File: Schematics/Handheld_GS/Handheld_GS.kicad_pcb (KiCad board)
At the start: 2 copper layers, 141.6 x 70 mm, 152 parts, among them IC1 P3T1755DPZ, J1 MB_A, J2 MB_B, J4 1S Li-Ion Cell, J5 Speaker, J6 MB_A, J7 1S Li-Ion Cell, J9 DB_B, Q1 AO3401A, Q2 MMBT3904, Q3 MMBT3904, Q4 AO3400A, Q5 AO3400A, Q6 AO3401A, Q7 AO3401A, SW1 SW_ENTER, SW2 SW_BACK, SW3 SW_DOWN, SW4 SW_UP, SW5 SW_ESP_BOOT_MODE, SW6 SW_ESP_RESET, SW7 PWR, U1 CP2102N-Axx-xQFN28, U10 TPB4056B2X-ES1R, U11 AMS1117-3.3, U12 NAU7802SGI, U2 ESP32-S3-WROOM-1, U3 RFM95W-915S2, U4 TPS63001DRCR, U5 LM66100DCKR, U6 LM66100DCKR, U7 MAX98357AETE_T, U8 TPS63001DRCR, U9 AMS1117-3.3

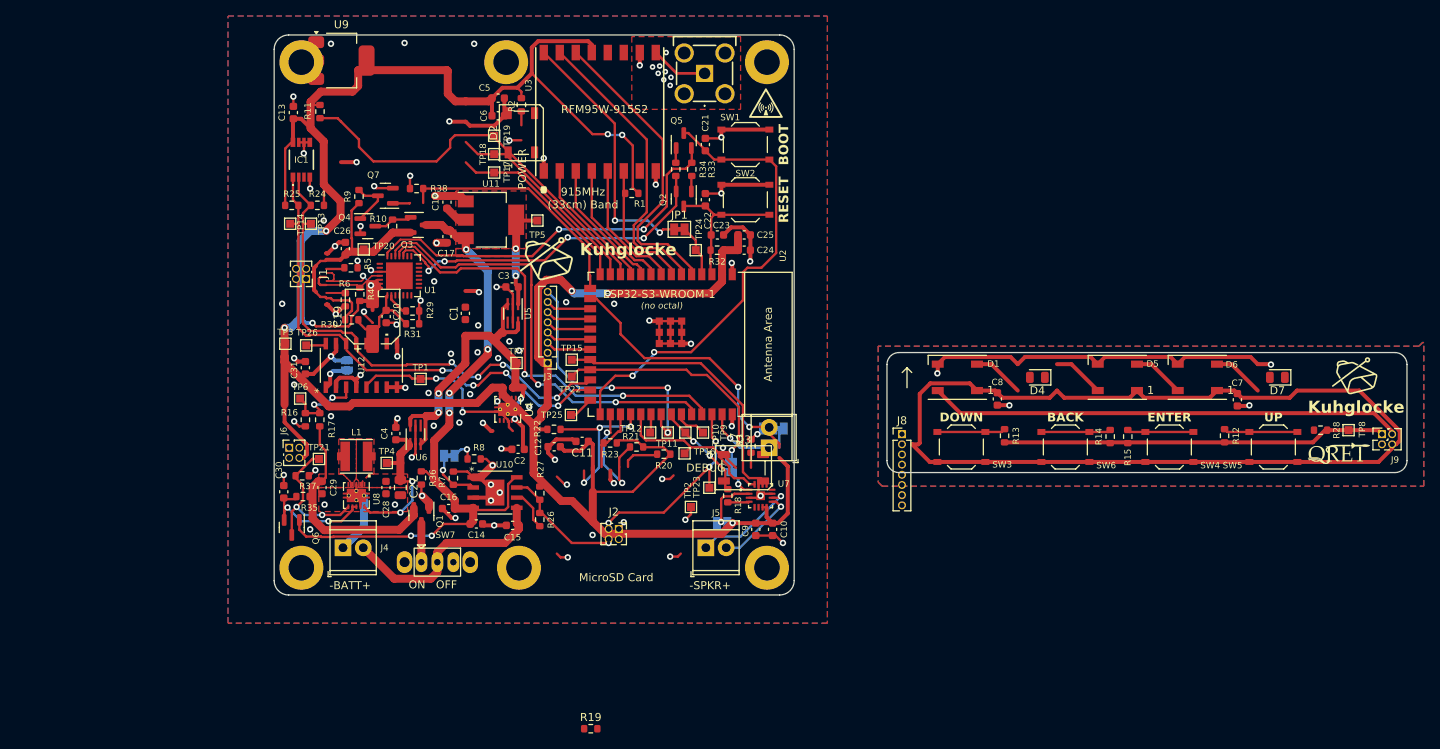
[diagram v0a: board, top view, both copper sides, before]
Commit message: Updated ground station with suggest changes and more, routing done
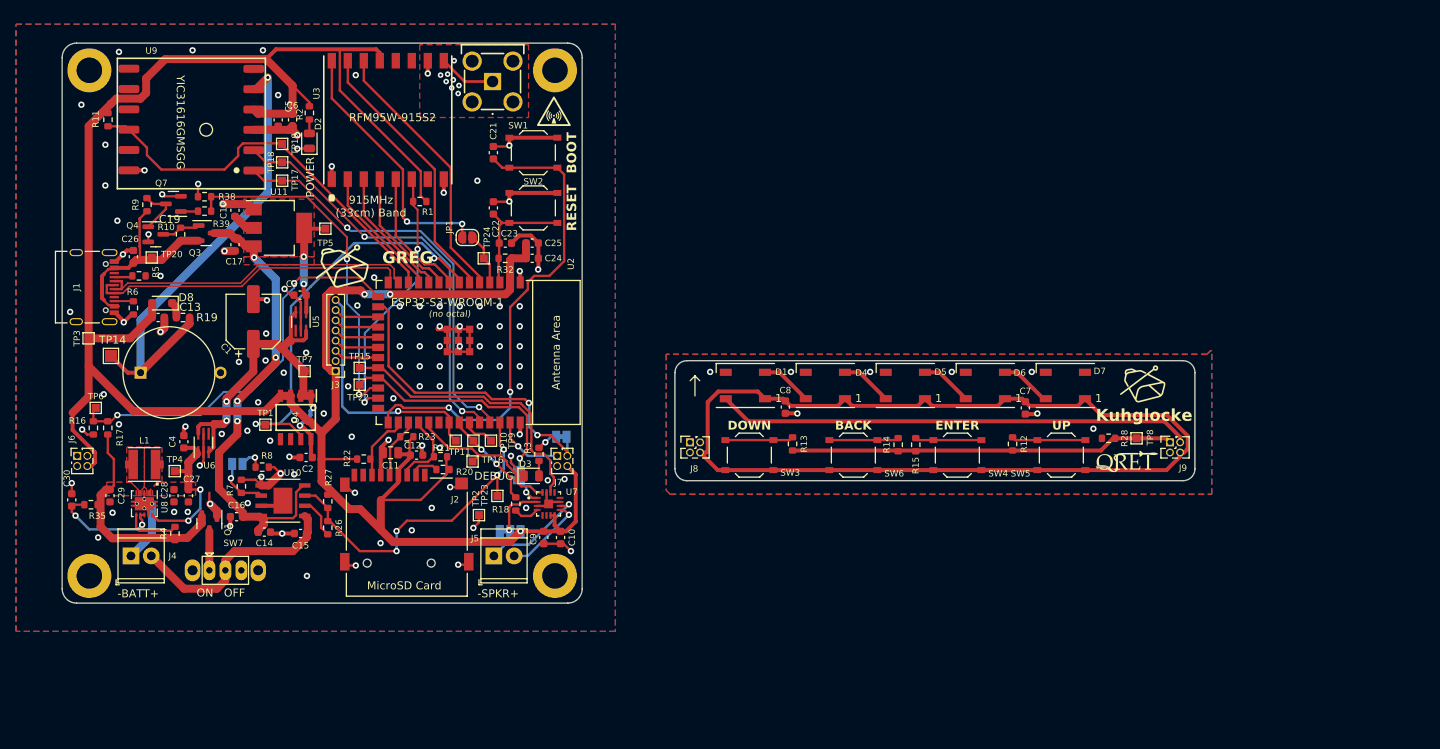
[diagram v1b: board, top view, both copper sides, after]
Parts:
- removed C20: 10uF, Capacitor_SMD:C_0603_1608Metric
- removed C31: 4.7uF, Capacitor_SMD:C_0603_1608Metric
- removed H5, H6: MountingHole, MountingHole:MountingHole_3.2mm_M3_ISO14580_Pad
- removed IC1: P3T1755DPZ, footprints:P3T1755DPZ
- removed JP6: DIO2_EN, Jumper:SolderJumper-2_P1.3mm_Open_RoundedPad1.0x1.5mm
- removed Q2: MMBT3904, Package_TO_SOT_SMD:SOT-23
- removed Q5: AO3400A, Package_TO_SOT_SMD:SOT-23
- removed Q6: AO3401A, Package_TO_SOT_SMD:SOT-23
- removed R24: 100k, Resistor_SMD:R_0603_1608Metric
- removed R25, R33, R34, R36, R37: 10k, Resistor_SMD:R_0603_1608Metric
- removed R29: 1.5k, Resistor_SMD:R_0603_1608Metric
- removed R30, R31: 5.1k, Resistor_SMD:R_0603_1608Metric
- removed TP12: TP_VUSB, TestPoint:TestPoint_Pad_1.0x1.0mm
- removed TP13: TP_VPSU, TestPoint:TestPoint_Pad_1.0x1.0mm
- removed TP21: TP_SDA, TestPoint:TestPoint_Pad_1.0x1.0mm
- removed TP25: GPS_TX, TestPoint:TestPoint_Pad_1.0x1.0mm
- removed TP26: GPS_RX, TestPoint:TestPoint_Pad_1.0x1.0mm
- removed U1: CP2102N-Axx-xQFN28, Package_DFN_QFN:QFN-28-1EP_5x5mm_P0.5mm_EP3.35x3.35mm
- removed U12: NAU7802SGI, NAU7802SGI:SOI16_NAU7802SGI_NUV
- added D8: 1N5819WS, Diode_SMD:D_SOD-323_HandSoldering, F.Cu at (35.1, 71.4)
- added R39: 510, Resistor_SMD:R_0603_1608Metric, F.Cu at (40.4, 59.9)
- C1: value 1uF -> 100uF; footprint Capacitor_SMD:C_0603_1608Metric -> Capacitor_SMD:CP_Elec_6.3x5.9
- C10: value 1uF -> 10uF
- C11: value 0.1uF -> 47uF; footprint Capacitor_SMD:C_0603_1608Metric -> Capacitor_SMD:C_0805_2012Metric
- C12, C16, C2, C22: value 1uF -> 0.1uF
- C14, C15, C23, C8: value 10uF -> 1uF
- C17, C18, C24, C26, C29: value 0.1uF -> 10uF
- C19: value 100uF -> 330mF; footprint Capacitor_SMD:CP_Elec_6.3x5.9 -> footprints:CB5R5334HF-ZJP
- C25, C5: value 10uF -> 0.1uF
- C27: value 47uF -> 10uF; footprint Capacitor_SMD:C_0805_2012Metric -> Capacitor_SMD:C_0603_1608Metric
- C4: value 0.1uF -> 1uF
- C6: value 10uF -> 4.7uF
- D2: value WS2812B -> INT_PWR_LED (RED); footprint LED_SMD:LED_WS2812B_PLCC4_5.0x5.0mm_P3.2mm -> LED_SMD:LED_0805_2012Metric
- D3: value WS2812B -> DB_LED (GRN); footprint LED_SMD:LED_WS2812B_PLCC4_5.0x5.0mm_P3.2mm -> LED_SMD:LED_0805_2012Metric
- D4: value DB_LED (GRN) -> WS2812B; footprint LED_SMD:LED_0805_2012Metric -> LED_SMD:LED_WS2812B_PLCC4_5.0x5.0mm_P3.2mm
- D7: value INT_PWR_LED (RED) -> WS2812B; footprint LED_SMD:LED_0805_2012Metric -> LED_SMD:LED_WS2812B_PLCC4_5.0x5.0mm_P3.2mm
- J1: value MB_A -> USB_C_Female_USB2_Small; footprint Connector_PinSocket_1.27mm:PinSocket_2x02_P1.27mm_Vertical -> footprints:USB_C_DB-108PWB
- J2: value MB_B -> MSD-1-A MicroSD Slot; footprint Connector_PinSocket_1.27mm:PinSocket_2x02_P1.27mm_Vertical -> footprints:MicroSD_MSD-1-A
- J7: value 1S Li-Ion Cell -> MB_B; footprint TerminalBlock_TE-Connectivity:TerminalBlock_TE_282834-2_1x02_P2.54mm_Horizontal -> Connector_PinSocket_1.27mm:PinSocket_2x02_P1.27mm_Vertical
- J8: value ~ -> DB_A; footprint Connector_PinHeader_1.27mm:PinHeader_1x08_P1.27mm_Vertical -> footprints:HPH2-A-04-UA_PINS
- JP1: value DB_LED_EN -> DIO2_EN; footprint Jumper:SolderJumper-2_P1.3mm_Bridged_Pad1.0x1.5mm -> Jumper:SolderJumper-2_P1.3mm_Open_RoundedPad1.0x1.5mm
- JP2: value FastCharge -> Gain; footprint Jumper:SolderJumper-2_P1.3mm_Open_Pad1.0x1.5mm -> Jumper:SolderJumper-3_P1.3mm_Bridged12_Pad1.0x1.5mm_NumberLabels
- JP3: value ADC_REFP -> SPK_DIN
- JP4: value SPK_DIN -> FastCharge; footprint Jumper:SolderJumper-2_P1.3mm_Bridged_Pad1.0x1.5mm -> Jumper:SolderJumper-2_P1.3mm_Open_Pad1.0x1.5mm
- JP5: value Gain -> DB_LED_EN; footprint Jumper:SolderJumper-3_P1.3mm_Bridged12_Pad1.0x1.5mm_NumberLabels -> Jumper:SolderJumper-2_P1.3mm_Bridged_Pad1.0x1.5mm
- Q3: value MMBT3904 -> AO3401A
- Q7: value AO3401A -> AO3400A
- R10: value 2k -> 51k
- R11: value 1k -> 10k
- R13: value 51k -> 1k
- R14: value 2.4k -> 2k
- R15: value 1k -> 5.6k
- R17: value 10k -> 20k
- R19: value 510 -> 100R
- R2: value 22k -> 1.8k
- R22: value 100k -> 10k
- R23: value 51k -> 10k
- R26: value 1.8k -> 10k
- R27: value 4.7k -> 10k
- R28: value 4.7k -> 1k
- R3: value 47k -> 10k
- R35: value 10k -> 100
- R38: value 10k -> 100k
- R4: value 1k -> 100k
- R5: value 10k -> 5.1k
- R6: value 3.9k -> 5.1k
- R7: value 100 -> 2.4k
- R8: value 100k -> 3.9k
- R9: value 5.6k -> 100k
- SW1: value SW_ENTER -> SW_ESP_BOOT_MODE
- SW2: value SW_BACK -> SW_ESP_RESET
- SW4: value SW_UP -> SW_ENTER
- SW5: value SW_ESP_BOOT_MODE -> SW_UP
- SW6: value SW_ESP_RESET -> SW_BACK
- TP1: value IO39 -> TP_ISENSE
- TP10: value TP_BTN -> IO41
- TP11: value PSU_EN -> IO40
- TP14: value CHRG_STAT -> BKP; footprint TestPoint:TestPoint_Pad_1.0x1.0mm -> TestPoint:TestPoint_Pad_1.5x1.5mm
- TP15: value TP_MUX -> I2S_LRCLK
- TP16: value ADC_LDO -> I2S_BLCK
- TP17: value TP_ISENSE -> GPS_RX
- TP18: value TP_GND -> GPS_TX
- TP19: value TP_3V3 -> GPS_RST
- TP2: value IO40 -> TP_GND
- TP20: value TP_SCL -> 5V_RAW
- TP22: value 5V_RAW -> I2S_DIN
- TP23: value GPS_RST -> CHRG_STAT
- TP24: value B_SENSE -> IO4
- TP3: value IO41 -> TP_3V3
- TP4: value IO42 -> TP_VPSU
- TP5: value IO45 -> TP_VUSB
- TP6: value IO4 -> B_SENSE
- TP7: value I2S_LRCLK -> TP_MUX
- TP8: value I2S_BLCK -> TP_BTN
- TP9: value I2S_DIN -> IO42
- U4: value TPS63001DRCR -> ACS70331EOLC; footprint Package_SON:Texas_DRC0010J_ThermalVias -> footprints:SOIC127P600X175-8N
- U9: value AMS1117-3.3 -> YIC31616GMSGG GPS; footprint Package_TO_SOT_SMD:SOT-223-3_TabPin2 -> footprints:YIC31616GMSGG
- moved R19 72.4 mm to (37.7, 73.2)
- moved R4 37.8 mm to (36.7, 100.2), turned to 90 degrees
- moved C13 30.7 mm to (34.6, 73.2), turned to 0 degrees
- moved TP14 27.8 mm to (28.7, 78.0), turned to 0 degrees
- moved R20 27.7 mm to (70.2, 92.2)
- moved C5 27.6 mm to (49.6, 48.5), turned to 90 degrees
- moved J9 26.5 mm to (161.1, 88.8)
- moved R14 26.5 mm to (127.1, 89.1)
- moved C15 26.5 mm to (52.4, 100.2)
- moved C16 26.5 mm to (44.4, 98.1)
- moved C27 26.5 mm to (38.4, 95.5)
- moved C3 26.5 mm to (52.3, 70.4)
- moved J3 26.5 mm to (56.8, 79.9)
- moved R38 26.5 mm to (40.4, 58.1)
- moved TP7 26.5 mm to (52.9, 79.9)
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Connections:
- C1 pad 1: GND -> V_MUX
- C1 pad 2: ESP32_EN -> GND
- C10 pad 1: +5V -> +3.3V
- C11 pad 1: GND -> +3.3V
- C11 pad 2: +5V -> GND
- C12 pad 1: V_REGUSB -> +3.3V
- C13 pad 1: V_PSU -> +3.3V
- C14 pad 1: V_PSU -> +5V
- C15 pad 1: V_PSU -> GND
- C15 pad 2: GND -> RAW_BATT
- C16 pad 2: RAW_BATT -> +5V
- C17 pad 1: GND -> +5V
- C17 pad 2: GPIO0 -> GND
- C18 pad 1: GND -> V_REGUSB
- C18 pad 2: ESP32_EN -> GND
- C19 pad 1: V_MUX -> /GPS_BCKP
- C2 pad 1: GND -> V_MUX
- C2 pad 2: Net-(U1-VBUS) -> GND
- C21 pad 1: V_MUX -> GND
- C21 pad 2: GND -> GPIO0
- C22 pad 2: +3.3V -> ESP32_EN
- C23 pad 1: V_REGUSB -> GND
- C23 pad 2: GND -> ESP32_EN
- C26 pad 1: +3.3V -> GND
- C26 pad 2: GND -> 5V_RAW
- C27 pad 1: +3.3V -> V_PSU
- C28 pad 1: GND -> V_PSU
- C28 pad 2: 5V_RAW -> GND
- C29 pad 1: +3.3V -> +BATT
- C3 pad 1: GND2 -> V_REGUSB
- C3 pad 2: +3.3VA -> GND
- C30 pad 1: GND -> Net-(U8-PS/SYNC)
- C30 pad 2: +3.3V -> GND
- C4 pad 1: +3.3V -> V_PSU
- C6 pad 1: +3.3V -> GND
- C6 pad 2: GND -> +3.3V
- C8 pad 1: +BATT -> GND2
- C8 pad 2: GND -> +3.3VA
- C9 pad 1: Net-(Q1-S) -> +3.3V
- D2 pad 1: +3.3VA -> GND
- D2 pad 2: Net-(D2-DOUT) -> Net-(D2-A)
- D3 pad 1: +3.3VA -> GND
- D3 pad 2: Net-(D3-DOUT) -> Net-(D3-A)
- D4 pad 1: GND -> +3.3VA
- D4 pad 2: Net-(D4-A) -> Net-(D4-DOUT)
- D5 pad 4: Net-(D3-DOUT) -> Net-(D4-DOUT)
- D6 pad 2: unconnected-(D6-DOUT-Pad2) -> Net-(D6-DOUT)
- D7 pad 1: GND -> +3.3VA
- D7 pad 2: Net-(D7-A) -> unconnected-(D7-DOUT-Pad2)
- J2 pad 1: BUTTONS -> unconnected-(J2-DAT2-Pad1)
- J2 pad 2: GND -> Net-(J2-DAT3/CD)
- J2 pad 3: ARGB_DATA -> CMD_SDMMC
- J3 pad 1: (no net) -> +3.3V
- J3 pad 2: (no net) -> GND
- J3 pad 3: (no net) -> MOSI_EINK
- J3 pad 4: (no net) -> SCK_EINK
- J3 pad 5: (no net) -> CS_EINK
- J3 pad 6: (no net) -> EINK_DC
- J3 pad 7: (no net) -> RESET_EINK
- J3 pad 8: (no net) -> EINK_BUSY
- J4 pad 1: (no net) -> GND
- J4 pad 2: (no net) -> RAW_BATT
- J6 pad 1: (no net) -> unconnected-(J6-Pad1)
- J6 pad 2: (no net) -> GND
- J6 pad 3: (no net) -> unconnected-(J6-Pad3)
- J6 pad 4: (no net) -> +3.3V
- J7 pad 1: GND -> BUTTONS
- J7 pad 2: RAW_BATT -> GND
- J8 pad 1: +3.3V -> unconnected-(J8-Pad1)
- J8 pad 2: GND -> GND2
- J8 pad 3: MOSI_EINK -> unconnected-(J8-Pad3)
- J8 pad 4: SCK_EINK -> +3.3VA
- J9 pad 1: (no net) -> BUTTONS_DB
- J9 pad 2: (no net) -> GND2
- J9 pad 3: (no net) -> ARGB_DATA_DB
- J9 pad 4: (no net) -> +3.3VA
- JP1 pad 1: ARGB_DATA -> Net-(JP1-A)
- JP1 pad 2: Net-(JP1-B) -> DIO2_RF
- JP2 pad 1: Net-(JP2-A) -> GND
- JP2 pad 2: Net-(JP2-B) -> Net-(JP2-C)
- JP3 pad 1: +3.3V -> Net-(JP3-A)
- JP3 pad 2: Net-(JP3-B) -> I2S_DIN_SPK
- JP4 pad 2: I2S_DIN_SPK -> Net-(JP4-B)
- JP5 pad 1: GND -> ARGB_DATA
- JP5 pad 2: Net-(JP5-C) -> Net-(JP5-B)
- Q1 pad 1: +5V -> GND
- Q1 pad 2: Net-(Q1-S) -> +BATT
- Q3 pad 1: Net-(Q3-B) -> Net-(Q3-G)
- Q3 pad 2: DTR -> 5V_RAW
- Q3 pad 3: GPIO0 -> +5V
- Q4 pad 3: Net-(Q4-D) -> Net-(Q3-G)
- Q7 pad 1: GND -> Net-(Q7-G)
- Q7 pad 2: +BATT -> GND
- Q7 pad 3: Net-(Q7-D) -> Net-(Q4-G)
- R1 pad 1: +3.3V -> RESET_RF
- R1 pad 2: ESP32_EN -> +3.3V
- R10 pad 1: BUTTONS_DB -> 5V_RAW
- R10 pad 2: Net-(R10-Pad2) -> Net-(Q3-G)
- R11 pad 1: Net-(R11-Pad1) -> +3.3V
- R11 pad 2: BUTTONS_DB -> GPS_RST
- R13 pad 1: GND -> Net-(R13-Pad1)
- R13 pad 2: Net-(Q1-D) -> BUTTONS_DB
- R14 pad 1: GND -> BUTTONS_DB
- R14 pad 2: Net-(JP2-B) -> Net-(R14-Pad2)
- R15 pad 1: GND2 -> Net-(R15-Pad1)
- R16 pad 1: DTR -> BATT_SENSE
- R16 pad 2: Net-(Q2-B) -> GND
- R17 pad 1: Net-(Q3-B) -> +BATT
- R17 pad 2: RTS -> BATT_SENSE
- R18 pad 1: 5V_OFF -> SPK_ON
- R18 pad 2: GND -> Net-(U7-SD_MODE)
- R19 pad 1: 5V_OFF -> Net-(D8-K)
- R19 pad 2: Net-(Q4-G) -> /GPS_BCKP
- R2 pad 1: Net-(U1-VBUS) -> Net-(D2-A)
- R2 pad 2: 5V_RAW -> +3.3V
- R20 pad 1: CHRG_STAT -> +3.3V
- R20 pad 2: +3.3V -> Net-(J2-DAT3/CD)
- R21 pad 1: Net-(U3-STBY) -> +3.3V
- R21 pad 2: CHRG_STAT -> CMD_SDMMC
- R22 pad 1: 5V_RAW -> +3.3V
- R22 pad 2: Net-(Q4-D) -> D0_SDMMC
- R23 pad 1: 5V_RAW -> +3.3V
- R23 pad 2: Net-(Q5-D) -> CLK_SDMMC
- R26 pad 1: Net-(D7-A) -> Net-(U10-STBY)
- R26 pad 2: +3.3V -> CHRG_STAT
- R27 pad 1: I2C_SCL -> CHRG_STAT
- R28 pad 1: +3.3V -> GND2
- R28 pad 2: I2C_SDA -> BUTTONS_DB
- R3 pad 1: GND -> Net-(D3-A)
- R3 pad 2: Net-(U1-VBUS) -> Net-(JP5-B)
- R32 pad 2: CMD_SDMMC -> ESP32_EN
- R35 pad 1: +3.3V -> +BATT
- R35 pad 2: Net-(J9-DAT3/CD) -> Net-(U8-PS/SYNC)
- R38 pad 1: BATT_SENSE -> 5V_OFF
- R4 pad 1: Net-(U1-~{RST}) -> +BATT
- R4 pad 2: GND -> Net-(U8-EN)
- R5 pad 1: Net-(D4-A) -> Net-(J1-CC1)
- R5 pad 2: Net-(JP1-B) -> GND
- R6 pad 1: Net-(JP2-A) -> Net-(J1-CC2)
- R7 pad 1: +BATT -> GND
- R7 pad 2: Net-(Q1-S) -> Net-(JP4-B)
- R8 pad 1: +5V -> Net-(JP4-A)
- R9 pad 1: Net-(R9-Pad1) -> 5V_RAW
- R9 pad 2: BUTTONS_DB -> Net-(Q4-G)
- SW1 pad 1: +3.3VA -> GND
- SW1 pad 2: Net-(R9-Pad1) -> GPIO0
- SW2 pad 1: +3.3VA -> GND
- SW2 pad 2: Net-(R10-Pad2) -> ESP32_EN
- SW3 pad 2: Net-(R11-Pad1) -> Net-(R13-Pad1)
- SW4 pad 2: Net-(R12-Pad1) -> Net-(R15-Pad1)
- SW5 pad 1: GND -> +3.3VA
- SW5 pad 2: GPIO0 -> Net-(R12-Pad1)
- SW6 pad 1: GND -> +3.3VA
- SW6 pad 2: ESP32_EN -> Net-(R14-Pad2)
- SW7 pad 1: Net-(Q7-D) -> Net-(Q1-D)
- TP1 pad 1: Net-(U2-MTCK/GPIO39/CLK_OUT3/SUBSPICS1) -> CURR_SENSE
- TP10 pad 1: BUTTONS_DB -> SPK_ON
- TP11 pad 1: Net-(Q1-D) -> EINK_BUSY
- TP14 pad 1: CHRG_STAT -> /GPS_BCKP
- TP15 pad 1: V_MUX -> I2S_LRCLK_SPK
- TP16 pad 1: Net-(U7-AVDD/LDO) -> I2S_BCLK_SPK
- TP17 pad 1: CURR_SENSE -> UART1_GPS_TX
- TP18 pad 1: GND -> UART1_GPS_RX
- TP19 pad 1: +3.3V -> GPS_RST
- TP2 pad 1: EINK_BUSY -> GND
- TP20 pad 1: I2C_SCL -> 5V_RAW
- TP22 pad 1: 5V_RAW -> I2S_DIN_SPK
- TP23 pad 1: GPS_RST -> CHRG_STAT
- TP24 pad 1: BATT_SENSE -> DIO2_RF
- TP3 pad 1: SPK_ON -> +3.3V
- TP4 pad 1: MISO_EINK -> V_PSU
- TP5 pad 1: Net-(U2-GPIO45) -> V_REGUSB
- TP6 pad 1: DIO2_RF -> BATT_SENSE
- TP7 pad 1: I2S_LRCLK_SPK -> V_MUX
- TP8 pad 1: I2S_BCLK_SPK -> BUTTONS_DB
- TP9 pad 1: I2S_DIN_SPK -> MISO_EINK
- U10 pad 1: (no net) -> GND
- U10 pad 2: (no net) -> Net-(JP4-B)
- U10 pad 3: (no net) -> GND
- U10 pad 4: (no net) -> +5V
- U10 pad 5: (no net) -> RAW_BATT
- U10 pad 6: (no net) -> Net-(U10-STBY)
- U10 pad 7: (no net) -> CHRG_STAT
- U10 pad 8: (no net) -> +5V
- U10 pad 9: (no net) -> GND
- U11 pad 1: (no net) -> GND
- U11 pad 2: (no net) -> V_REGUSB
- U11 pad 3: (no net) -> +5V
- U2 pad 13: UART1_GPS_RX -> USB_D-
- U2 pad 14: UART1_GPS_TX -> USB_D+
- U2 pad 15: 5V_OFF -> BATT_SENSE
- U2 pad 24: I2C_SCL -> 5V_OFF
- U2 pad 25: I2C_SDA -> RESET_RF
- U2 pad 26: Net-(U2-GPIO45) -> unconnected-(U2-GPIO45-Pad26)
- U2 pad 28: CMD_SDMMC -> D0_SDMMC
- U2 pad 30: D0_SDMMC -> CMD_SDMMC
- U2 pad 32: Net-(U2-MTCK/GPIO39/CLK_OUT3/SUBSPICS1) -> unconnected-(U2-MTCK/GPIO39/CLK_OUT3/SUBSPICS1-Pad32)
- U2 pad 36: UART0_RX -> UART1_GPS_RX
- U2 pad 37: UART0_TX -> UART1_GPS_TX
- U2 pad 7: RESET_RF -> CURR_SENSE
- U3 pad 1: (no net) -> GND
- U3 pad 10: (no net) -> GND
- U3 pad 11: (no net) -> unconnected-(U3-DIO3-Pad11)
- U3 pad 12: (no net) -> unconnected-(U3-DIO4-Pad12)
- U3 pad 13: (no net) -> +3.3V
- U3 pad 14: (no net) -> DIO0_RF
- U3 pad 15: (no net) -> DIO1_RF
- U3 pad 16: (no net) -> Net-(JP1-A)
- U3 pad 2: (no net) -> MISO_RF
- U3 pad 3: (no net) -> MOSI_RF
- U3 pad 4: (no net) -> SCK_RF
- U3 pad 5: (no net) -> CS_RF
- U3 pad 6: (no net) -> RESET_RF
- U3 pad 7: (no net) -> unconnected-(U3-DIO5-Pad7)
- U3 pad 8: (no net) -> GND
- U3 pad 9: (no net) -> Net-(AE1-A)
- U4 pad 1: V_PSU -> V_MUX
- U4 pad 2: /LA -> V_MUX
- U4 pad 3: GND -> +3.3V
- U4 pad 4: /LB -> +3.3V
- U4 pad 5: +BATT -> GND
- U4 pad 6: Net-(Q1-D) -> unconnected-(U4-NC-Pad6)
- U4 pad 7: Net-(Q1-S) -> CURR_SENSE
- U4 pad 8: Net-(Q1-S) -> V_MUX
- U7 pad 1: (no net) -> Net-(JP3-A)
- U7 pad 10: (no net) -> Net-(J5-Pin_1)
- U7 pad 11: (no net) -> GND
- U7 pad 14: (no net) -> I2S_LRCLK_SPK
- U7 pad 15: (no net) -> GND
- U7 pad 16: (no net) -> I2S_BCLK_SPK
- U7 pad 17: (no net) -> GND
- U7 pad 2: (no net) -> Net-(JP2-C)
- U7 pad 3: (no net) -> GND
- U7 pad 4: (no net) -> Net-(U7-SD_MODE)
- U7 pad 7: (no net) -> +3.3V
- U7 pad 8: (no net) -> +3.3V
- U7 pad 9: (no net) -> Net-(J5-Pin_2)
- U8 pad 1: (no net) -> V_PSU
- U8 pad 10: (no net) -> V_PSU
- U8 pad 11: (no net) -> GND
- U8 pad 2: (no net) -> /LA
- U8 pad 3: (no net) -> GND
- U8 pad 4: (no net) -> /LB
- U8 pad 5: (no net) -> +BATT
- U8 pad 6: (no net) -> Net-(U8-EN)
- U8 pad 7: (no net) -> Net-(U8-PS/SYNC)
- U8 pad 8: (no net) -> Net-(U8-PS/SYNC)
- U8 pad 9: (no net) -> GND
- U9 pad 1: GND -> UART1_GPS_TX
- U9 pad 2: V_REGUSB -> UART1_GPS_RX
- U9 pad 3: +5V -> GND
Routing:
- net (no net): track 1809.2 -> 0.00 mm, vias 137 -> 0
- net +3.3V: track 12.8 -> 306.8 mm
- net +3.3VA: track 0.00 -> 137.9 mm
- net GND: track 57.4 -> 146.0 mm, vias 16 -> 126
- net /GPS_BCKP: track 0.00 -> 59.8 mm, vias 0 -> 1
- net GPIO0: track 1.31 -> 61.0 mm, vias 1 -> 2
- net +5V: track 1.57 -> 58.1 mm, vias 1 -> 4
- net UART0_RX: track 56.0 -> 0.00 mm, vias 2 -> 0
- net UART0_TX: track 55.4 -> 0.00 mm, vias 2 -> 0
- net UART1_GPS_RX: track 0.00 -> 52.4 mm, vias 0 -> 2
- net CURR_SENSE: track 0.00 -> 51.9 mm, vias 0 -> 2
- net BATT_SENSE: track 0.00 -> 50.9 mm, vias 0 -> 2
- net GPS_RST: track 0.00 -> 50.1 mm
- net UART1_GPS_TX: track 2.55 -> 52.4 mm, vias 0 -> 2
- net V_MUX: track 0.00 -> 48.5 mm, vias 0 -> 4
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- added copper zone on F.Cu, net +BATT
- added copper zone on B.Cu, net GND
- added copper zone on F.Cu, net V_PSU
- added copper zone on F.Cu, net V_REGUSB
- removed copper zone on F.Cu, net (none)
- removed copper zone on F.Cu, net +3.3V
- removed copper zone on F.Cu, net 5V_RAW
- removed copper zone on B.Cu, net EINK_BUSY
- removed copper zone on F.Cu, net EINK_BUSY
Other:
- board text added: "GREG"
- board text added: "GRREG MB Rev 1.2 (Ground Station Mainboard) QRET March 2026 Tristan Alderson Kennan Bays Owen Price"
- board text added: "TARPON PCB"
- board text removed: "ADC 3.3V REF"
- board text removed: "Kuhglocke MB Rev 1.0 (Ground Station Mainboard) QRET May 2024 Kennan Bays Owen Price"

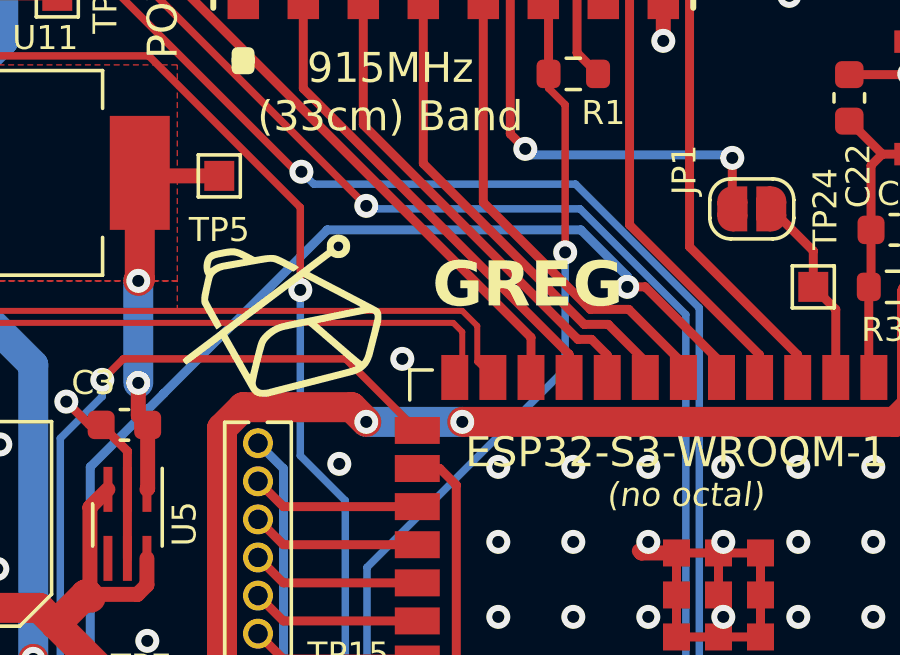
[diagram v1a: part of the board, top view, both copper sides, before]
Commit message: Update Silkscreen and Added some 3D models
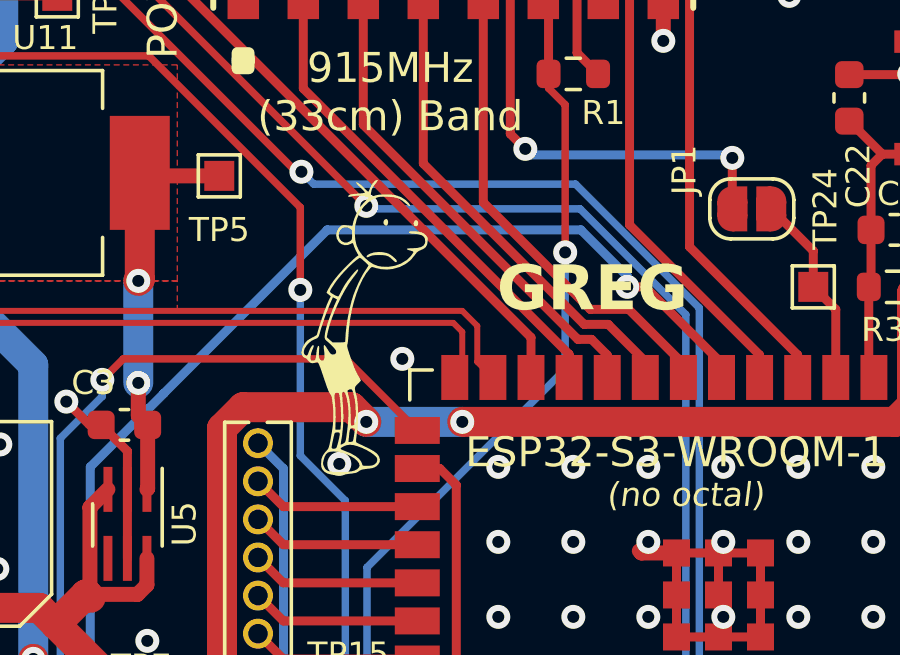
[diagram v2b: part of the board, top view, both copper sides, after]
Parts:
- added G***: LOGO, LOGO, F.Cu at (60.2, 67.2)

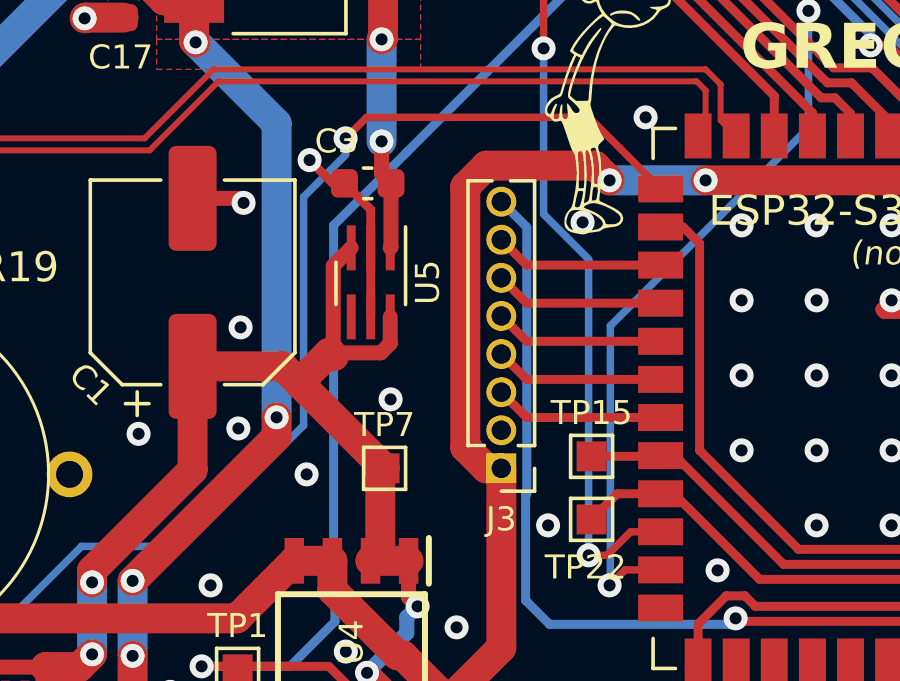
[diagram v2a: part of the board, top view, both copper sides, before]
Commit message: added silkscreen for eink pins
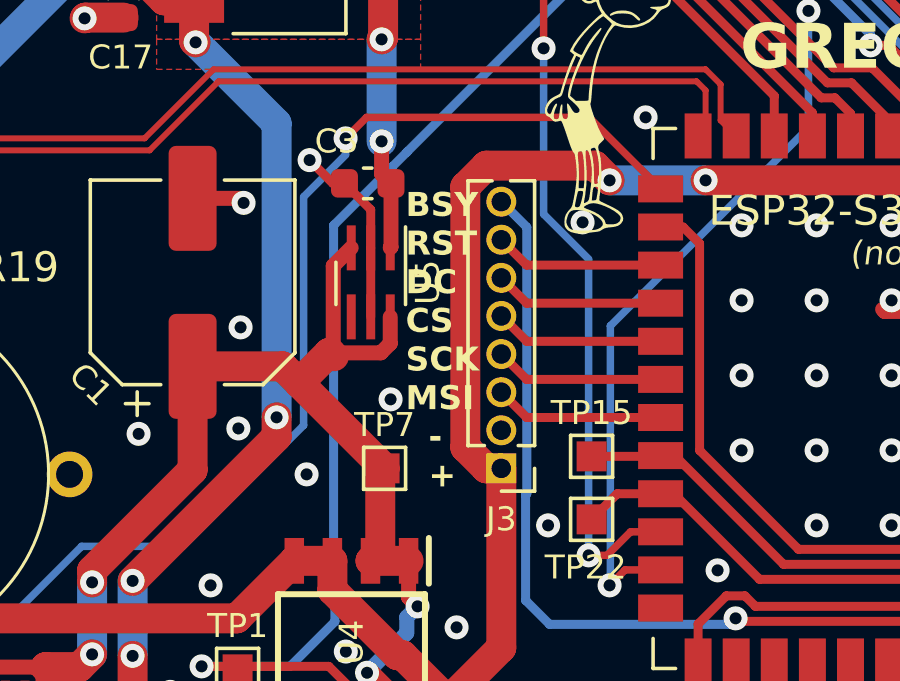
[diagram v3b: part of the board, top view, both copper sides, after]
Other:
- board text added: "BSY RST DC CS SCK MSI - +"
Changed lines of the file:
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@@
+		)
+	)
+	(gr_text "BSY\nRST\nDC\nCS\nSCK\nMSI\n  -\n  +\n"
+		(at 53.6 80.6 0)
+		(layer "F.SilkS")
+		(effects
+			(font
+				(size 0.8 0.8)
+				(thickness 0.15)
+				(bold yes)
+			)
+			(justify left bottom)
 		)
 	)
